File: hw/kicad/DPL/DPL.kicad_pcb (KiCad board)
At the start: 2 copper layers, 96 x 89.9 mm, 48 parts, among them J0 Programer, J1 DPL1, J2 DPL2, J3 DPL3, J4 DPL4, J5 DPL5, J6 DPL6, J7 USB_B_Micro, J8 BATT, J9 Level shifter, Q1 IRF540N, Q2 IRF540N, Q3 IRF540N, Q4 IRF540N, Q5 IRF540N, Q6 IRF540N, SW1 SW_Reed, SW2 SW_Reed, SW3 SW_Reed, SW4 SW_Reed, SW5 SW_Reed, SW6 SW_Reed, U0 SAMD21E, U1 Payload, U2 AP7215-33YG-13, Y1 32.768kHz

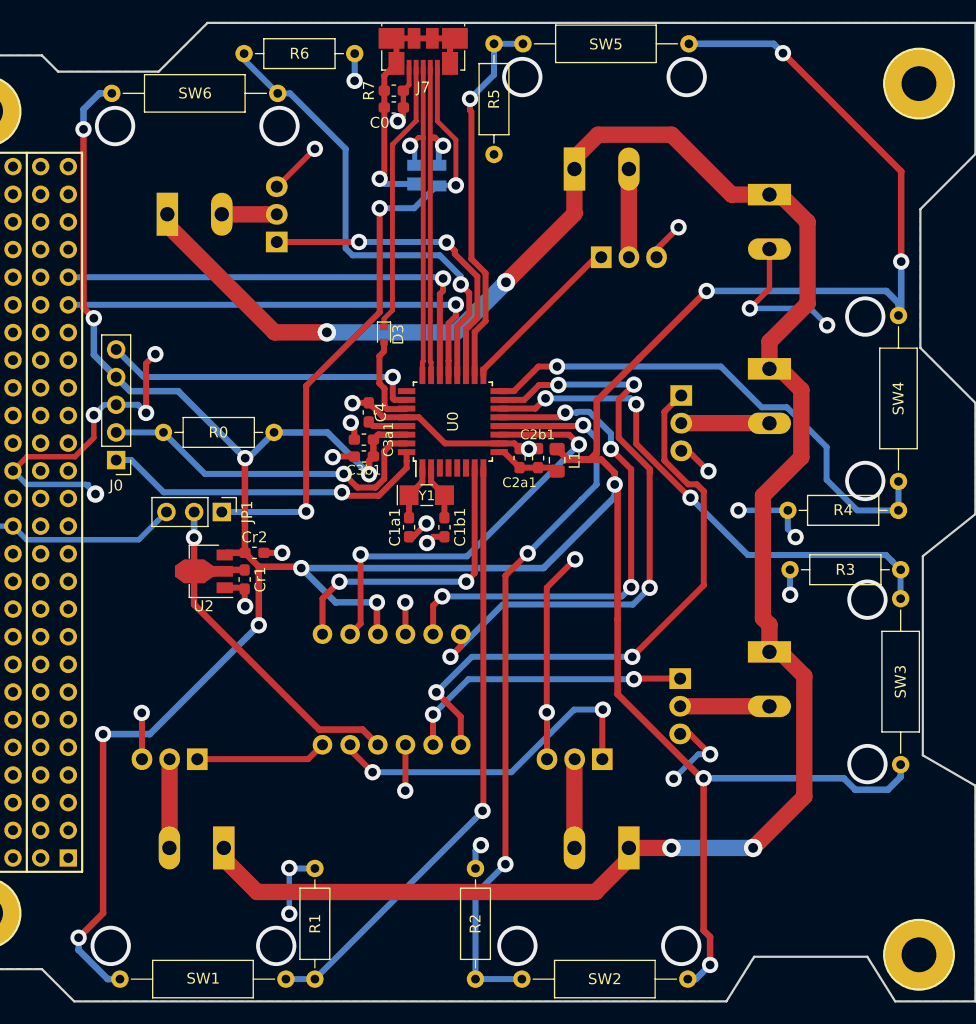
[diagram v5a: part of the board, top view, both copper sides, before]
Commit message: Increased the pad size of some vias. Rerouted some tracks.
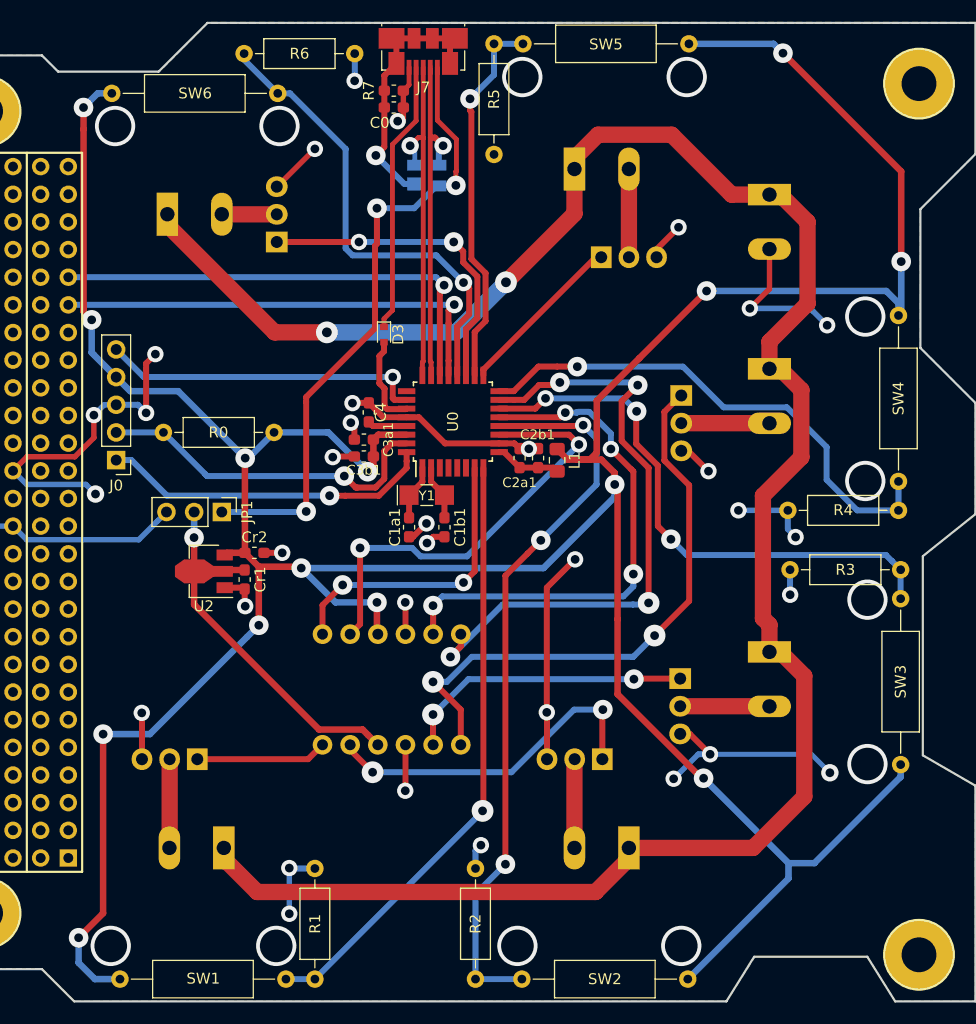
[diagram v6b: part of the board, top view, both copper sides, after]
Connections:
- U1 pad : (no net) -> GND
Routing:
- net GND: track 153.5 -> 165.2 mm, vias 32 -> 33
- net /DPL_STATUS3: track 48.6 -> 51.5 mm
- net /LV4: track 56.8 -> 57.9 mm
- net /LV2: track 39.8 -> 40.7 mm
- net /usb/SHIELD: track 25.4 -> 24.7 mm
- net /LV3: track 47.7 -> 48.2 mm
- net /EN_DPL4: track 54.4 -> 53.9 mm
- net /3V3: track 330.0 -> 330.5 mm, vias 15 -> 14
- net /VBATT: vias 4 -> 2
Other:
- net class Battery: via_dia 1.7 -> 1.8
- net class Default: via_dia 1.5 -> 1.6
- net class PC104: via_dia 1.5 -> 1.6
- net class Power: via_dia 1.5 -> 1.8
- net class USB: via_dia 1.5 -> 1.6
